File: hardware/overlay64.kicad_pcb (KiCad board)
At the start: 2 copper layers, 36.8 x 49.5 mm, 23 parts, among them IC1 ATMEGA328P-P, P1 ISP, P2 MAIN, P3 CONTROL, P4 BYPASS, P5 INPUT, Q1 BC547B, U1 LM1881, Y1 20MHz

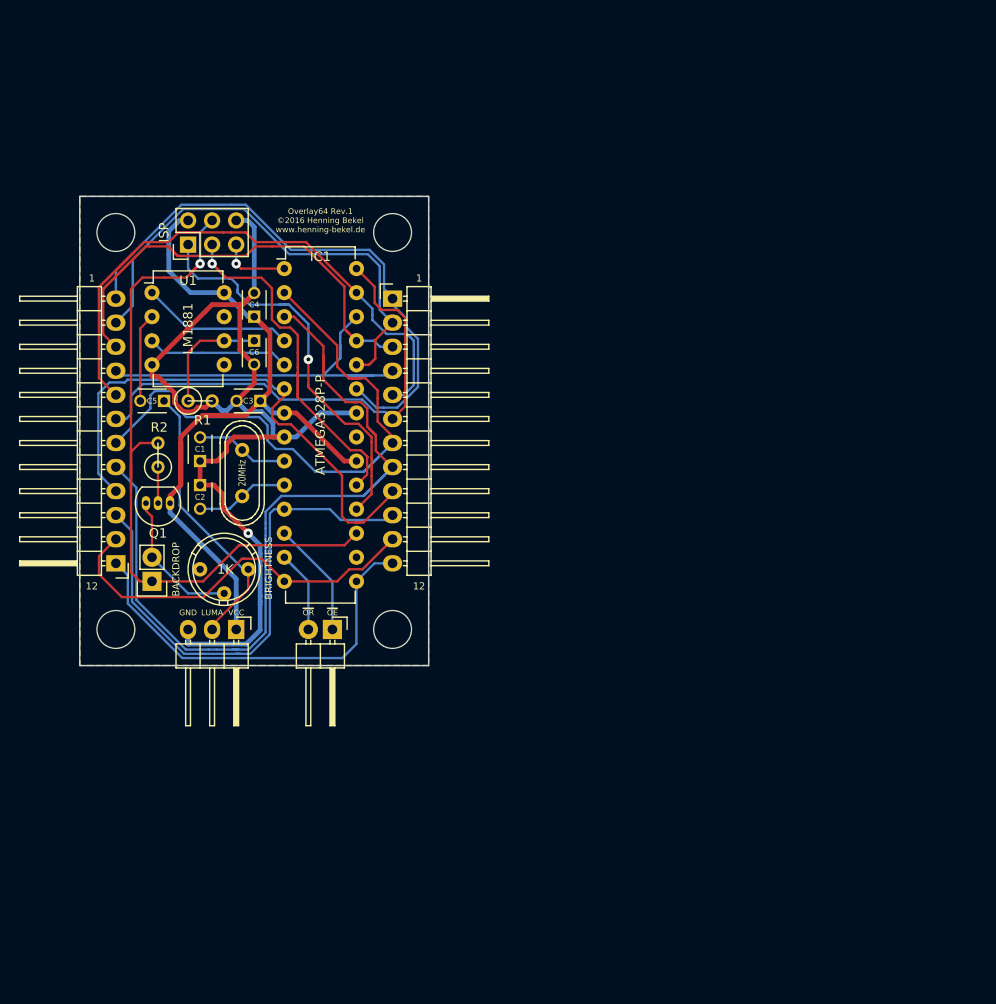
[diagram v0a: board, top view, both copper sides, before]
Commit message: Hardware: Fixed orientation/wiring for brightness pot
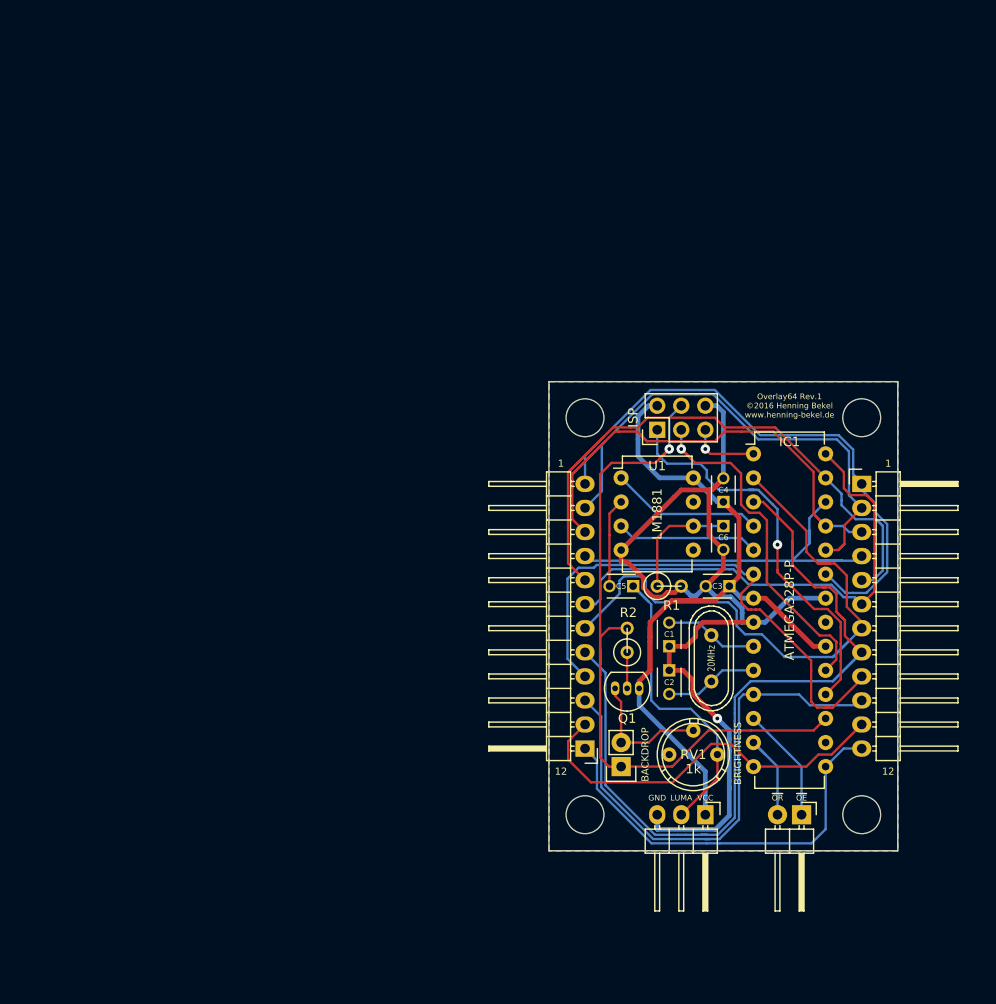
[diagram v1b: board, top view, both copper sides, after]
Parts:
- removed 1K: 1k, Potentiometers:Potentiometer_Bourns_3339P_Angular_ScrewUp
- removed H1, H2, H3, H4: MountingHole_4mm, Mounting_Holes:MountingHole_4mm
- added P6: HOLE, Mounting_Holes:MountingHole_4mm, F.Cu at (135.9, 79.2)
- added P7: HOLE, Mounting_Holes:MountingHole_4mm, F.Cu at (165.1, 79.2)
- added P8: HOLE, Mounting_Holes:MountingHole_4mm, F.Cu at (135.9, 121.2)
- added P9: HOLE, Mounting_Holes:MountingHole_4mm, F.Cu at (165.1, 121.2)
- added RV1: 1k, Potentiometers:Potentiometer_Bourns_3339P_Angular_ScrewUp, F.Cu at (144.8, 114.8)
- moved C1 53.3 mm to (144.8, 103.4)
- moved C2 53.3 mm to (144.8, 105.9)
- moved C3 53.3 mm to (151.1, 97.0)
- moved C4 53.3 mm to (150.5, 88.1)
- moved C5 53.3 mm to (141.0, 97.0)
- moved P2 53.3 mm to (148.6, 121.2)
- moved P3 53.3 mm to (158.8, 121.2)
- moved P4 53.3 mm to (165.1, 86.2)
- moved R1 53.3 mm to (144.8, 97.0)
- moved C6 53.3 mm to (150.5, 90.7)
- moved R2 53.3 mm to (140.3, 102.7)
- moved Y1 53.3 mm to (149.2, 104.6)
- moved IC1 53.3 mm to (153.7, 83.1)
- moved JP1 53.3 mm to (139.7, 116.1)
- moved P5 53.3 mm to (135.9, 114.2)
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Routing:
- net /LUMA: track 29.7 -> 34.1 mm
- net Net-(JP1-Pad2): track 15.4 -> 14.4 mm

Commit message: Hardware: Changed schematics for 1284p, removed pcb layout
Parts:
- removed C1, C2: 18pF, Capacitors_ThroughHole:C_Disc_D3_P2.5
- removed C3, C4, C5, C6: 100nF, Capacitors_ThroughHole:C_Disc_D3_P2.5
- removed IC1: ATMEGA328P-P, Housings_DIP:DIP-28_W7.62mm
- removed JP1: BACKDROP, Pin_Headers:Pin_Header_Straight_1x02
- removed P1: ISP, Pin_Headers:Pin_Header_Straight_2x03
- removed P2: MAIN, Pin_Headers:Pin_Header_Angled_1x03
- removed P3: CONTROL, Pin_Headers:Pin_Header_Angled_1x02
- removed P4: BYPASS, Pin_Headers:Pin_Header_Angled_1x12
- removed P5: INPUT, Pin_Headers:Pin_Header_Angled_1x12
- removed P6, P7, P8, P9: HOLE, Mounting_Holes:MountingHole_4mm
- removed Q1: BC547B, TO_SOT_Packages_THT:TO-92_Inline_Narrow_Oval
- removed R1: 680k, Discret:R1
- removed R2: 4k7, Discret:R1
- removed RV1: 1k, Potentiometers:Potentiometer_Bourns_3339P_Angular_ScrewUp
- removed U1: LM1881, Housings_DIP:DIP-8_W7.62mm
- removed Y1: 20MHz, Crystals:Crystal_HC49-U_Vertical
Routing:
- net GND: track 108.3 -> 0.00 mm, vias 1 -> 0
- net /IN7: track 91.0 -> 0.00 mm
- net VCC: track 85.7 -> 0.00 mm
- net /MOSI: track 82.5 -> 0.00 mm, vias 1 -> 0
- net /IN6: track 67.6 -> 0.00 mm
- net /IN4: track 66.8 -> 0.00 mm
- net /IN0: track 59.4 -> 0.00 mm
- net /IN8: track 57.9 -> 0.00 mm
- net /IN2: track 54.9 -> 0.00 mm
- net /IN9: track 54.6 -> 0.00 mm
- net /IN5: track 53.6 -> 0.00 mm
- net /IN1: track 53.1 -> 0.00 mm
- net /MISO: track 44.1 -> 0.00 mm, vias 1 -> 0
- net /IN11: track 43.1 -> 0.00 mm
- net /IN3: track 42.0 -> 0.00 mm
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- removed copper zone on B.Cu, net GND
- removed copper zone on F.Cu, net GND
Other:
- board outline removed
- board text removed: "1"
- board text removed: "12"
- board text removed: "20MHz"
- board text removed: "BACKDROP"
- board text removed: "BRIGHTNESS"
- board text removed: "C1"
- board text removed: "C2"
- board text removed: "C3"
- board text removed: "C4"
- board text removed: "C5"
- board text removed: "C6"
- board text removed: "GND"
- board text removed: "LUMA"
- board text removed: "Overlay64 Rev.1 ©2016 Henning Bekel www.henning-bekel.de"
- board text removed: "VCC"
- board text removed: "~OE"
- board text removed: "~OR"

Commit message: Hardware: Added custom components, started layout
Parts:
- added C1: 100nF, Capacitors_ThroughHole:C_Disc_D3_P2.5, F.Cu at (132.1, 83.2)
- added C2: 18pF, Capacitors_ThroughHole:C_Disc_D3_P2.5, F.Cu at (127.0, 88.9)
- added C3: 18pF, Capacitors_ThroughHole:C_Disc_D3_P2.5, F.Cu at (127.0, 91.4)
- added C4: 100nF, Capacitors_ThroughHole:C_Disc_D3_P2.5, F.Cu at (114.3, 68.6)
- added C5: 100nF, Capacitors_ThroughHole:C_Disc_D3_P2.5, F.Cu at (129.5, 68.6)
- added C6: 100nF, Capacitors_ThroughHole:C_Disc_D3_P2.5, F.Cu at (129.5, 63.5)
- added D1: 3.6V, custom:Diode-2.5mm-Vertical, F.Cu at (123.2, 109.2)
- added D2: 3.6V, custom:Diode-2.5mm-Vertical, F.Cu at (128.3, 109.2)
- added IC1: ATMEGA1284-P, Housings_DIP:DIP-40_W15.24mm, F.Cu at (134.6, 61.0)
- added JP1: BACKDROP, Pin_Headers:Pin_Header_Straight_1x02, F.Cu at (125.7, 76.2)
- added P1: USB, custom:USB-MINI-B-TH, F.Cu at (125.7, 119.4)
- added P2: INPUT, Pin_Headers:Pin_Header_Angled_1x16, F.Cu at (110.5, 104.1)
- added P3: CONTROL, Pin_Headers:Pin_Header_Angled_1x08, F.Cu at (151.1, 115.6)
- added P4: MAIN, Pin_Headers:Pin_Header_Angled_1x03, F.Cu at (118.1, 115.6)
- added P5: HOLE, Mounting_Holes:MountingHole_4mm, F.Cu at (88.9, 43.2)
- added P6: HOLE, Mounting_Holes:MountingHole_4mm, F.Cu at (175.3, 43.2)
- added P7: HOLE, Mounting_Holes:MountingHole_4mm, F.Cu at (156.2, 111.8)
- added P8: HOLE, Mounting_Holes:MountingHole_4mm, F.Cu at (78.7, 137.2)
- added P9: BYPASS, Pin_Headers:Pin_Header_Angled_1x16, F.Cu at (156.2, 66.0)
- added Q1: BC547B, TO_SOT_Packages_THT:TO-92_Inline_Narrow_Oval, F.Cu at (119.4, 78.7)
- added R1: 68, custom:R1, F.Cu at (124.5, 105.4)
- added R2: 68, custom:R1, F.Cu at (127.0, 105.4)
- added R3: 1k5, custom:R1, F.Cu at (121.9, 105.4)
- added R4: 4k7, custom:R1, F.Cu at (120.7, 74.9)
- added R5: 680k, custom:R1, F.Cu at (132.1, 67.3)
- added RV1: 1k, Potentiometers:Potentiometer_Bourns_3339P_Angular_ScrewUp, F.Cu at (118.1, 87.6)
- added U1: LM1881, Housings_DIP:DIP-8_W7.62mm, F.Cu at (119.4, 63.5)
- added Y1: 20MHz, Crystals:Crystal_HC49-U_Vertical, F.Cu at (130.8, 90.2)

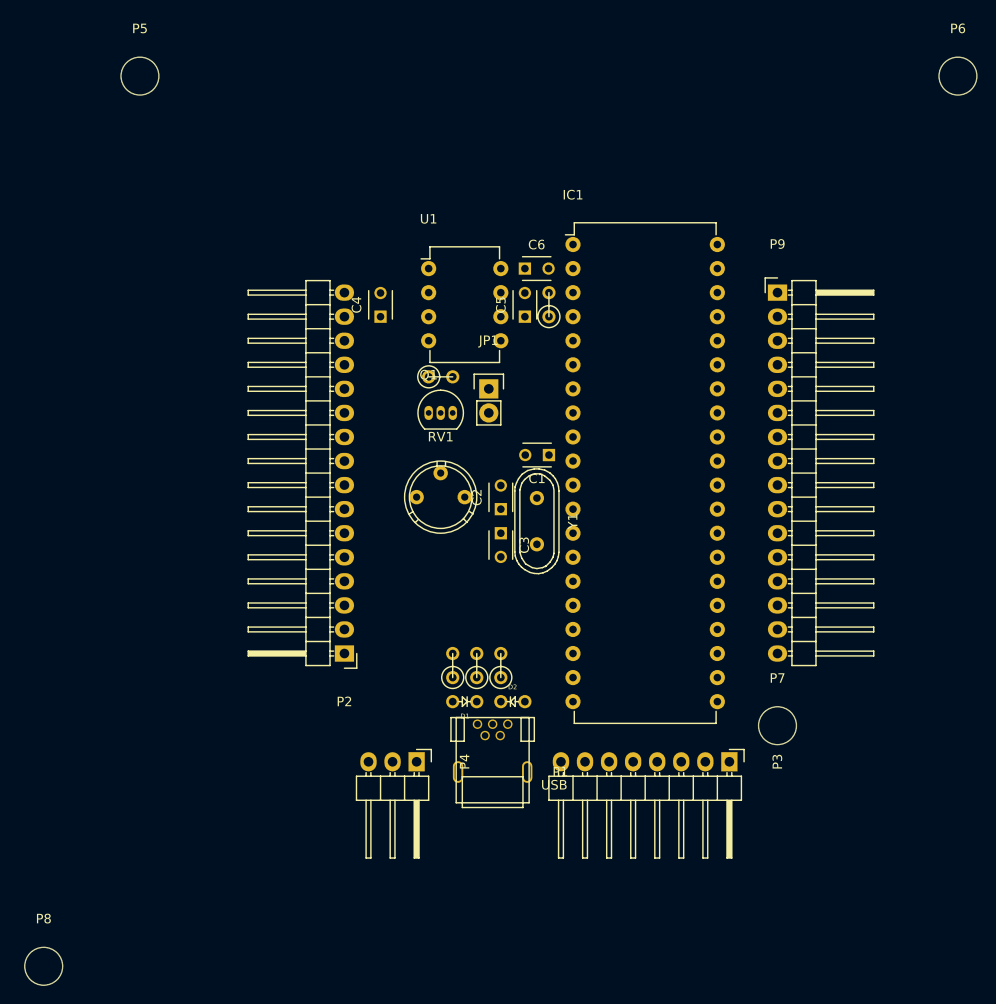
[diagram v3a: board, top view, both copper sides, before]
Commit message: Hardware: First draft of new pcb layout, autorouted
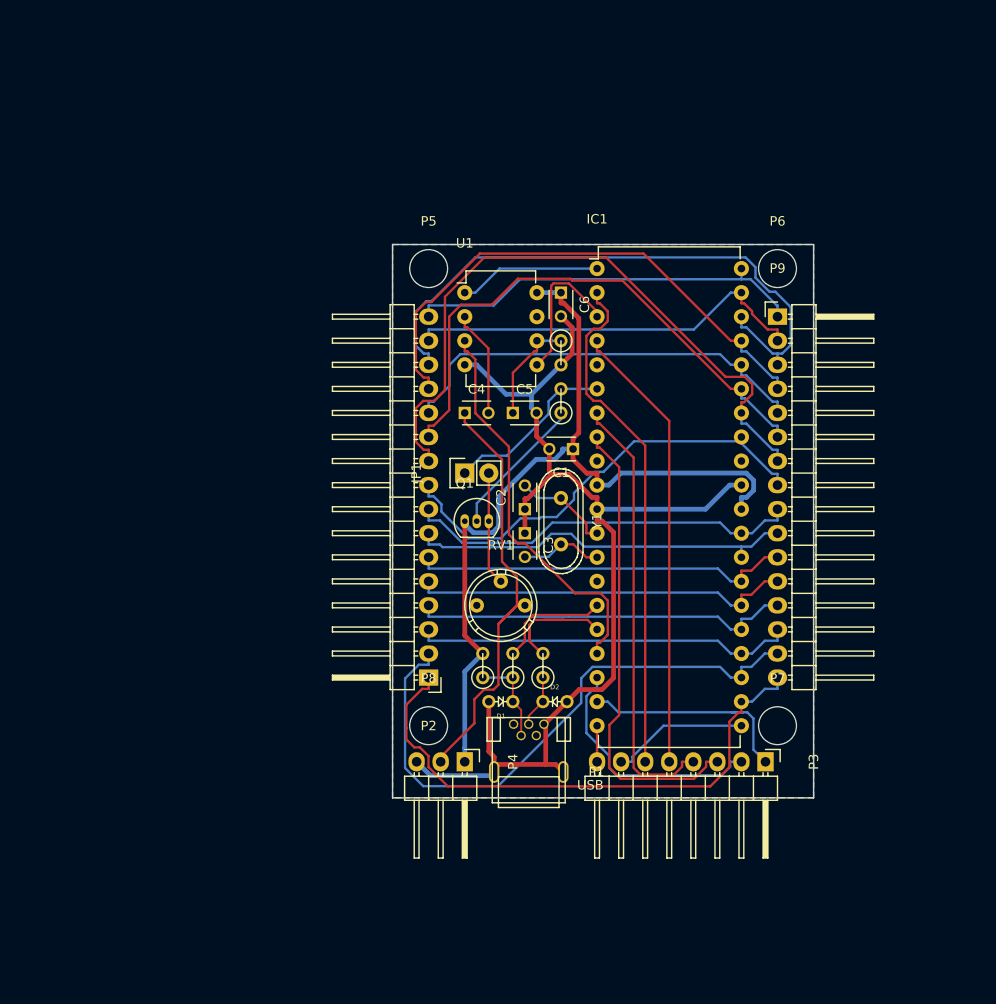
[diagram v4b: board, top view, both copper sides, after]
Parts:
- moved P8 47.9 mm to (119.4, 111.8)
- moved P5 36.6 mm to (119.4, 63.5)
- moved P6 27.9 mm to (156.2, 63.5)
- moved C4 13.5 mm to (123.2, 78.7), turned to 0 degrees
- moved RV1 13.1 mm to (124.5, 99.1)
- moved R4 13.0 mm to (133.3, 77.5), turned to 90 degrees
- moved Q1 12.0 mm to (123.2, 90.2)
- moved C5 10.2 mm to (128.3, 78.7), turned to 0 degrees
- moved JP1 9.25 mm to (123.2, 85.1), turned to 90 degrees
- moved P2 9.25 mm to (119.4, 106.7)
- moved R5 5.24 mm to (133.3, 72.4), turned to 270 degrees
- moved P4 5.08 mm to (123.2, 115.6)
- moved C6 4.58 mm to (133.3, 66.0), turned to 270 degrees
- moved U1 4.58 mm to (123.2, 66.0)
- moved D2 4.44 mm to (132.7, 109.2)
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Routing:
- net GND: track 0.00 -> 115.8 mm
- net VCC: track 0.00 -> 91.8 mm
- net /IN6: track 0.00 -> 70.7 mm
- net /IN2: track 0.00 -> 64.3 mm
- net /IN14: track 0.00 -> 62.8 mm
- net /IN15: track 0.00 -> 58.7 mm
- net /IN5: track 0.00 -> 58.4 mm
- net /IN3: track 0.00 -> 57.0 mm
- net /C0: track 0.00 -> 54.5 mm
- net /C3: track 0.00 -> 49.4 mm
- net /IN7: track 0.00 -> 48.2 mm
- net /C1: track 0.00 -> 47.8 mm
- net /C2: track 0.00 -> 46.7 mm
- net /LUMA: track 0.00 -> 46.5 mm
- net /IN4: track 0.00 -> 45.3 mm
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- added copper zone on B.Cu, net GND
- added copper zone on F.Cu, net GND
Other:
- board outline added: 44.5 x 58.4 mm
- net class USB added: clearance 0.127, trace_width 0.2, via_dia 1, via_drill 0.4

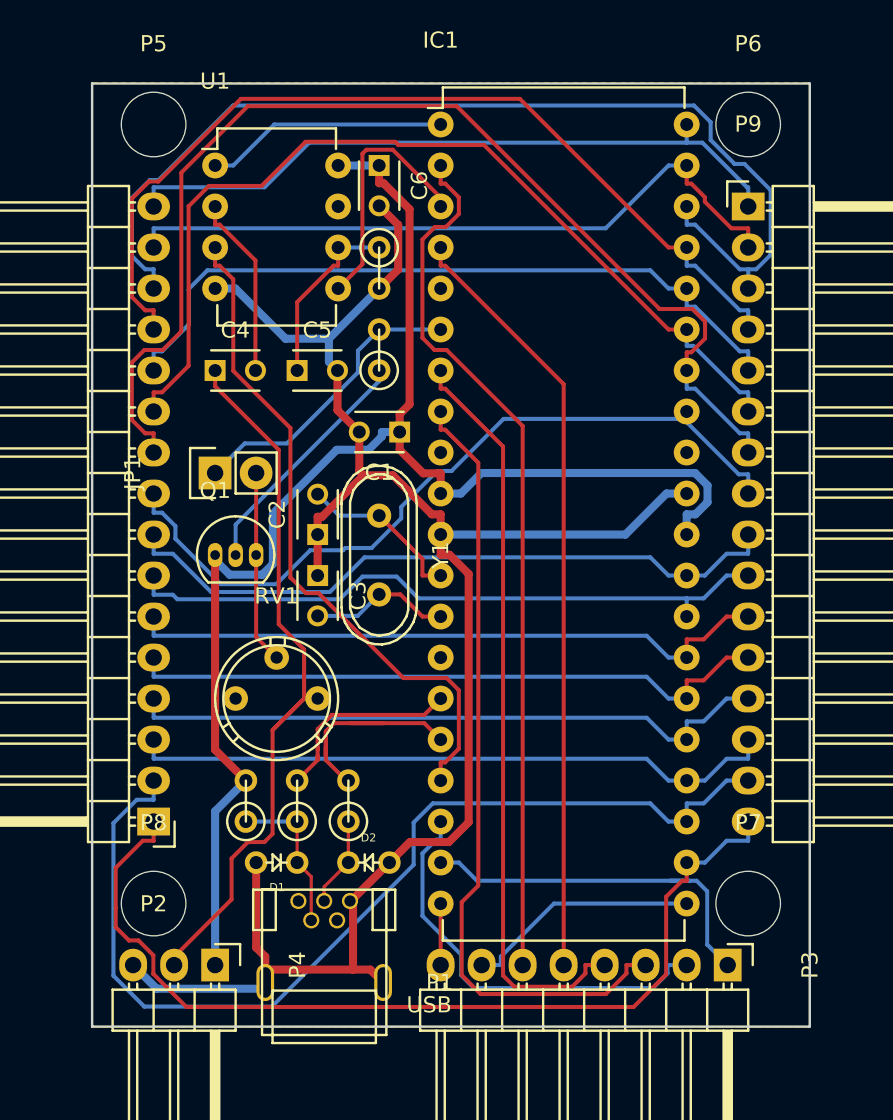
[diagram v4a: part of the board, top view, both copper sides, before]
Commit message: Hardware: Added jumpers for manually entering the bootloader
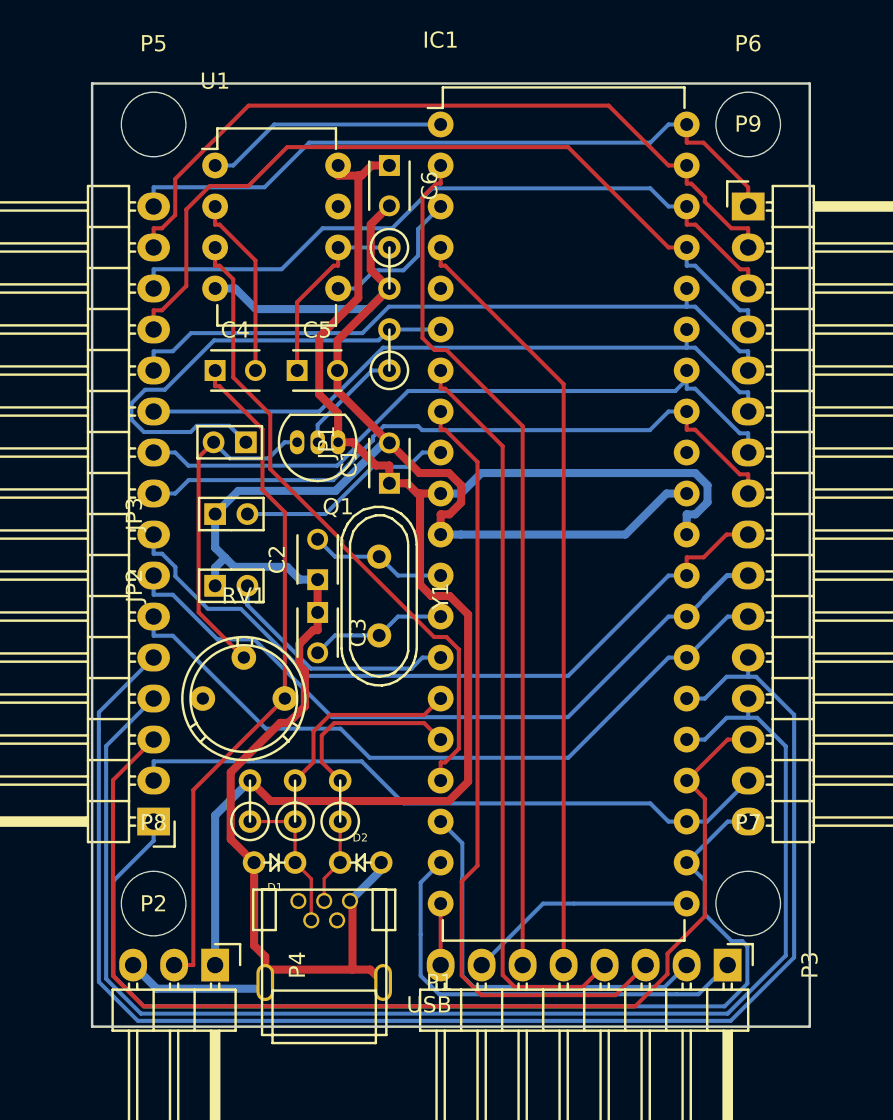
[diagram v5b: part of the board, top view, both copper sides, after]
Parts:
- added JP2: BOOT, custom:Pin_Header_Straight_1x02_Pitch2.00mm, F.Cu at (123.2, 92.1)
- added JP3: RESET, custom:Pin_Header_Straight_1x02_Pitch2.00mm, F.Cu at (123.2, 87.6)
- JP1: footprint Pin_Headers:Pin_Header_Straight_1x02 -> custom:Pin_Header_Straight_1x02_Pitch2.00mm
- moved Q1 10.3 mm to (130.8, 83.2), turned to 180 degrees
- moved C1 3.24 mm to (134.0, 85.7), turned to 90 degrees
- moved C2 2.79 mm to (129.5, 91.7)
- moved JP1 2.69 mm to (125.1, 83.2), turned to 270 degrees
- moved Y1 2.54 mm to (133.3, 92.7)
- moved C3 2.29 mm to (129.5, 93.7)
- moved RV1 2.03 mm to (122.4, 99.1)
- moved C6 0.64 mm to (134.0, 66.0)
- moved R4 0.64 mm to (134.0, 77.5)
- moved R5 0.64 mm to (134.0, 72.4)
- moved D2 0.51 mm to (132.2, 109.2)
- moved R2 0.51 mm to (130.9, 105.4)
- moved R3 0.25 mm to (125.3, 105.4)
- moved R1 0.13 mm to (128.1, 105.4)
- moved D1 0.13 mm to (126.9, 109.2)
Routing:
- net /IN11: track 40.3 -> 91.6 mm
- net /IN12: track 40.3 -> 84.6 mm
- net /IN13: track 40.3 -> 69.9 mm
- net /IN6: track 70.7 -> 43.0 mm
- net /IN14: track 62.8 -> 40.6 mm
- net /IN2: track 64.3 -> 44.0 mm
- net GND: track 115.8 -> 132.7 mm
- net /IN5: track 58.4 -> 41.9 mm
- net /BOOT: track 0.00 -> 15.1 mm
- net /~RESET: track 0.00 -> 13.5 mm
- net /MOSI: track 18.4 -> 30.0 mm
- net Net-(JP1-Pad2): track 12.0 -> 20.9 mm
- net Net-(Q1-Pad2): track 15.1 -> 6.92 mm
- net /IN9: track 41.0 -> 48.1 mm
- net /IN15: track 58.7 -> 65.5 mm
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
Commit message: Hardware: Prototype 2, rearranged, rerouted, added gerber files
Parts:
- D1, D2: value 3.6V -> 3.6; footprint custom:Diode-2.5mm-Vertical -> custom:D3
- IC1: value ATMEGA1284-P -> ATMEGA1284
- JP1, JP2, JP3: footprint custom:Pin_Header_Straight_1x02_Pitch2.00mm -> custom:Pin_Header_Straight_1x02
- R1, R2, R3, R4, R5: footprint custom:R1 -> Discret:R3
- moved RV1 15.5 mm to (125.1, 83.8)
- moved R4 13.6 mm to (121.9, 83.8)
- moved JP3 12.1 mm to (123.2, 99.7)
- moved JP1 11.6 mm to (123.2, 94.6), turned to 90 degrees
- moved Q1 8.64 mm to (125.7, 90.2)
- moved D1 5.24 mm to (122.8, 105.9), turned to 90 degrees
- moved JP2 5.08 mm to (123.2, 97.2)
- moved D2 3.75 mm to (134.0, 105.9), turned to 90 degrees
- moved C4 2.84 mm to (125.7, 77.5), turned to 180 degrees
- moved R5 2.54 mm to (134.0, 74.9)
- moved C5 1.27 mm to (128.3, 77.5)
- moved P5 0.76 mm to (119.4, 64.3)
- moved P6 0.76 mm to (156.2, 64.3)
- moved R1 0.57 mm to (128.4, 105.9)
- moved R2 0.57 mm to (131.2, 105.9)
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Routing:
- net /IN8: track 45.8 -> 101.0 mm
- net /IN11: track 91.6 -> 42.3 mm
- net /IN12: track 84.6 -> 41.4 mm
- net VCC: track 98.3 -> 85.9 mm
- net /~RESET: track 13.5 -> 25.6 mm, vias 0 -> 1
- net /IN3: track 51.0 -> 41.8 mm
- net /IN9: track 48.1 -> 38.9 mm
- net /LUMA: track 42.3 -> 51.3 mm
- net /IN2: track 44.0 -> 50.6 mm
- net /MOSI: track 30.0 -> 36.3 mm
- net /IN1: track 47.6 -> 42.0 mm
- net Net-(IC1-Pad16): track 11.4 -> 6.61 mm
- net GND: track 132.7 -> 137.3 mm
- net /IN15: track 65.5 -> 61.8 mm
- net Net-(JP1-Pad2): track 20.9 -> 17.2 mm
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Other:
- outline, holes or cut-outs redrawn
- board text added: "overlay64 2nd prototype by henning"
